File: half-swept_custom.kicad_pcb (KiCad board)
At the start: 2 copper layers, 108.6 x 86.9 mm, 24 parts, among them J2 AudioJack4dpb, SW10 SW_Push, SW11 SW_Push, SW12 SW_Push, SW14 SW_Push, SW15 SW_Push, SW16 SW_Push, SW17 SW_Push, SW18 SW_Push, SW2 SW_Push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

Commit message: Add silkscreen switch picture to half-swept
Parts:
- added REF**: silk_pg1232_bottom, silkscreens:pg1232_bottom, B.Cu at (57.5, 76.0)
- added REF**: silk_pg2132_top, silkscreens:pg1232_top, F.Cu at (57.5, 75.0)

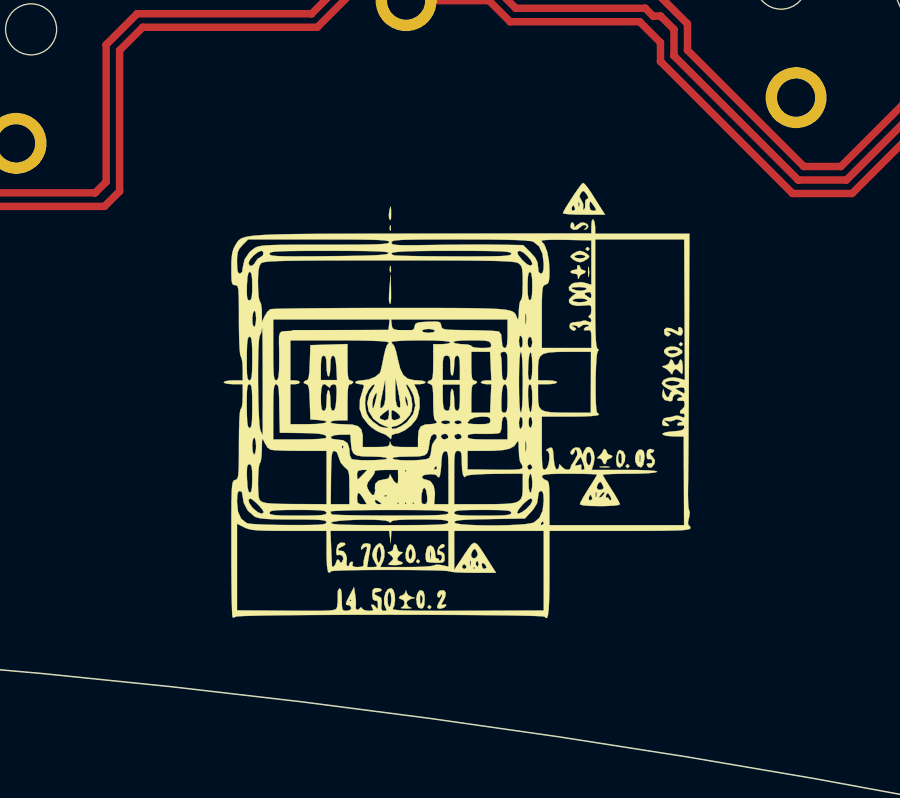
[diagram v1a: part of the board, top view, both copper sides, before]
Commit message: Add half swept boards with silkscreen
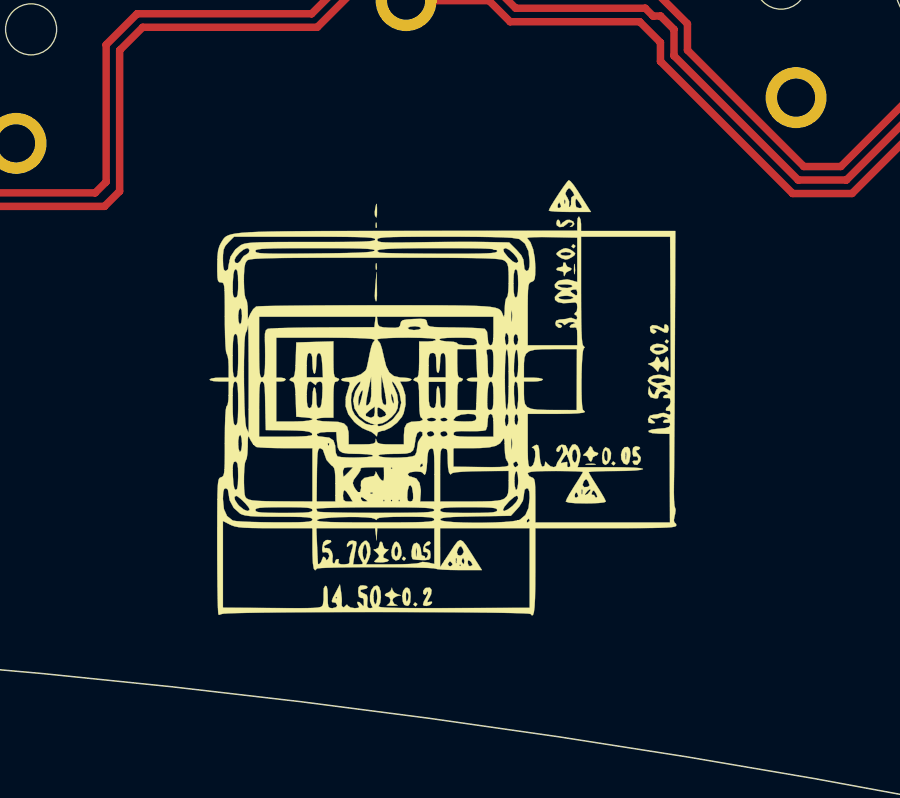
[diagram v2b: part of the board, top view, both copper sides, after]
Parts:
- moved REF** 1.66 mm to (59.1, 75.7)
- moved REF** 0.48 mm to (57.0, 74.9)

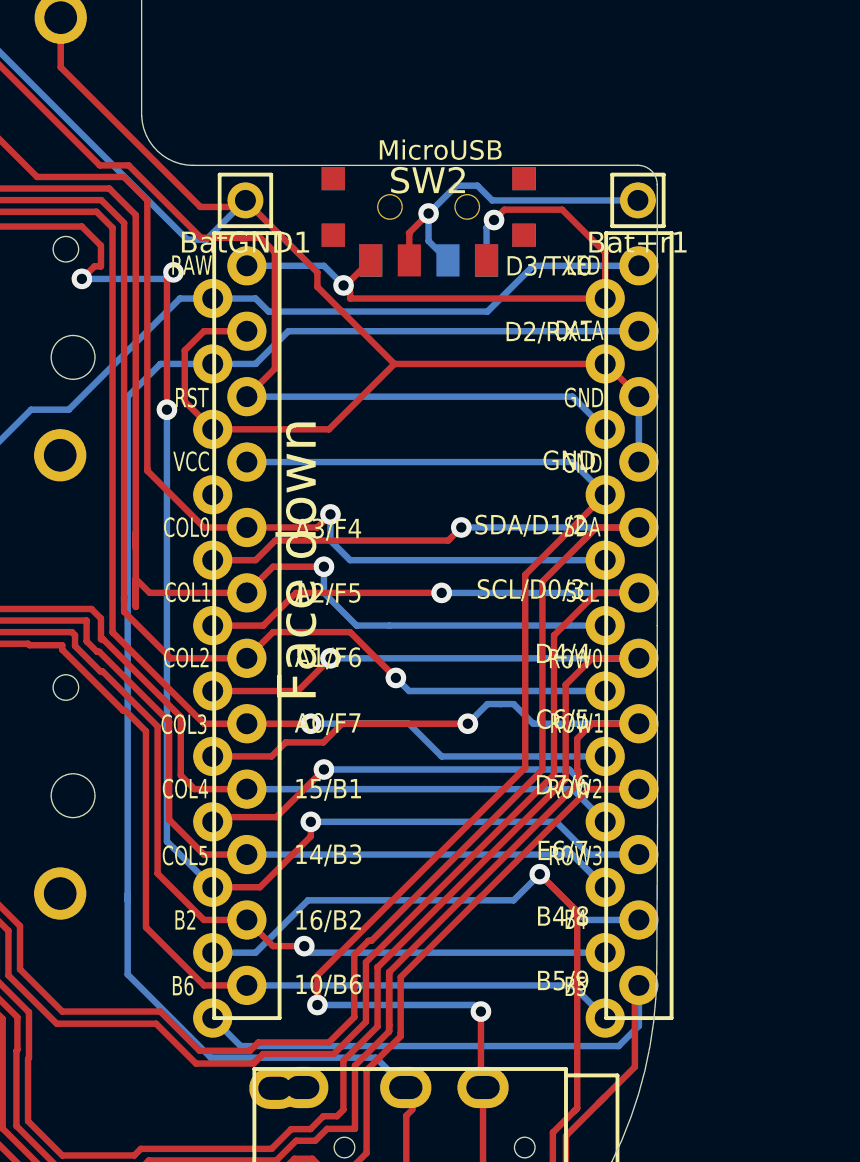
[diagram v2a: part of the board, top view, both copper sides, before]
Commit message: Remove battery pads and overlapping silkscreen
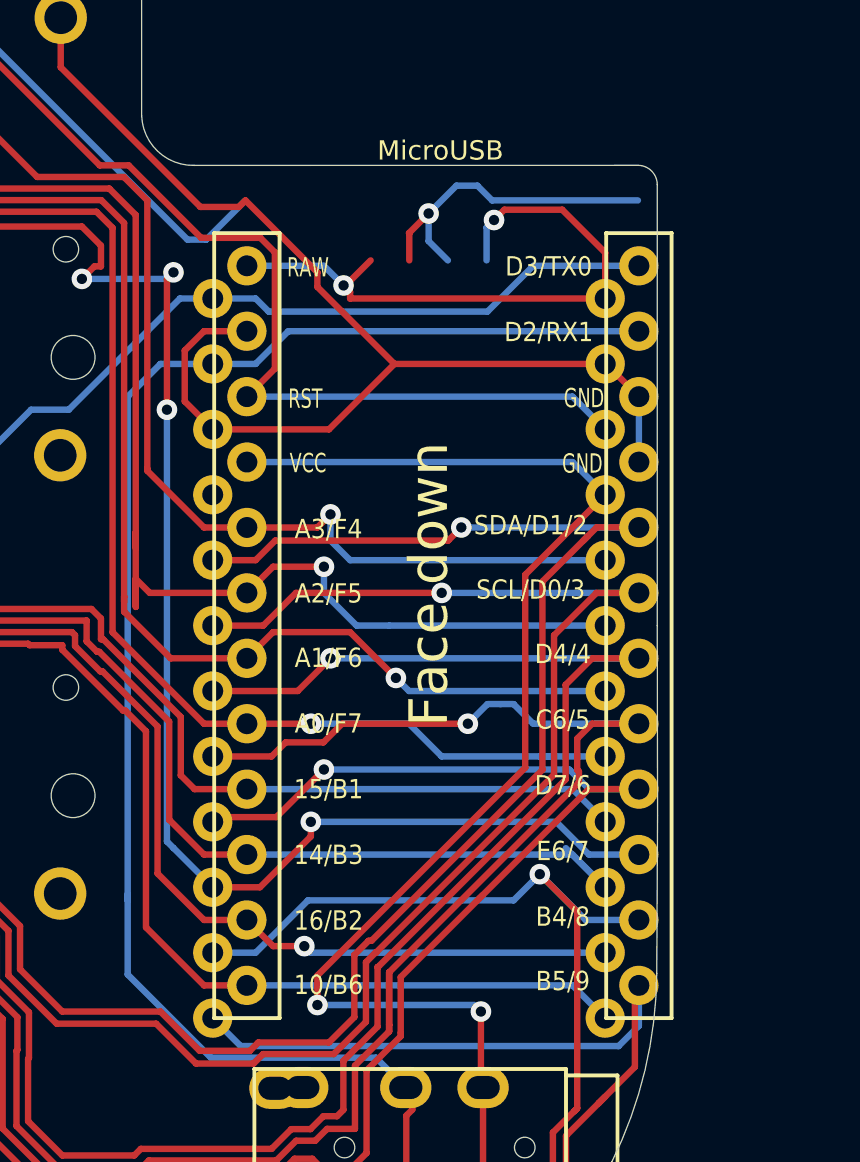
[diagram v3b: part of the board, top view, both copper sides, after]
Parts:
- removed Bat+r1, BatGND1: MountingHole_Pad, kbd:1pin_conn
- removed the SW2 at (113.3, 41.1)
- removed SW_POWERR1: SW_SPDT, Kailh:SPDT_C128955

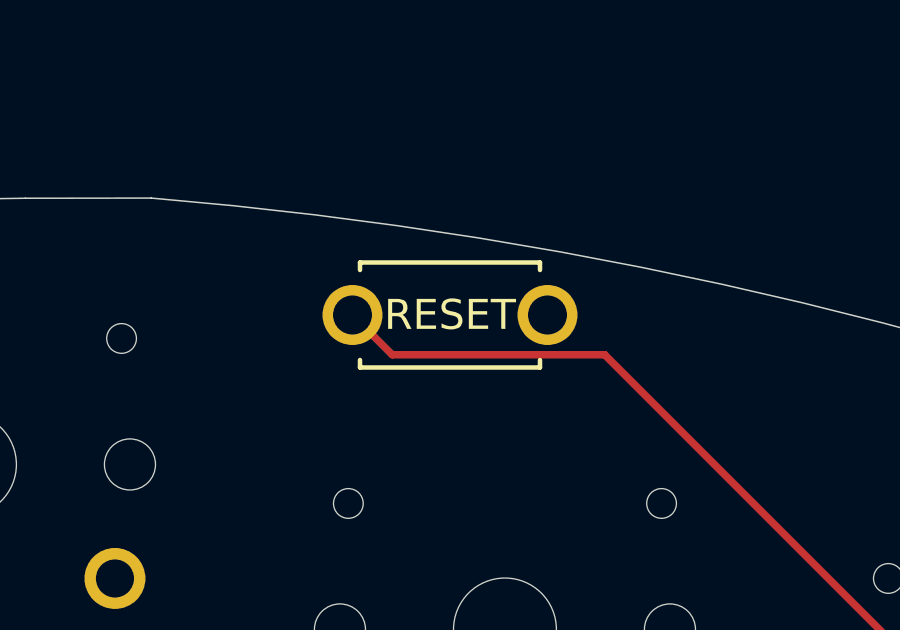
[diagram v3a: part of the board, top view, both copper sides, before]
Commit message: Remove reset switch
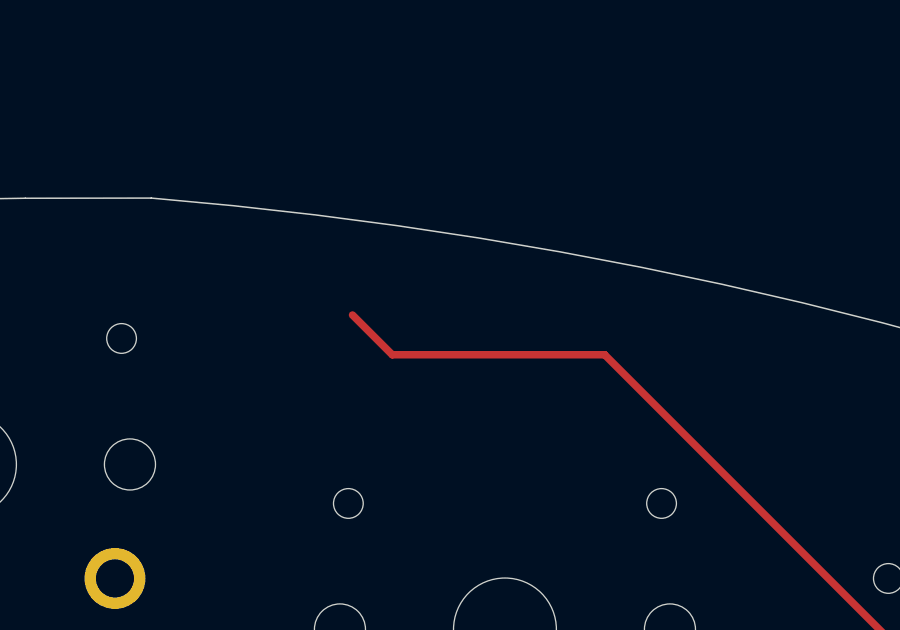
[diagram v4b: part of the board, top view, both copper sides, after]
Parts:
- removed RSW1: SW_Push, kbd:ResetSW

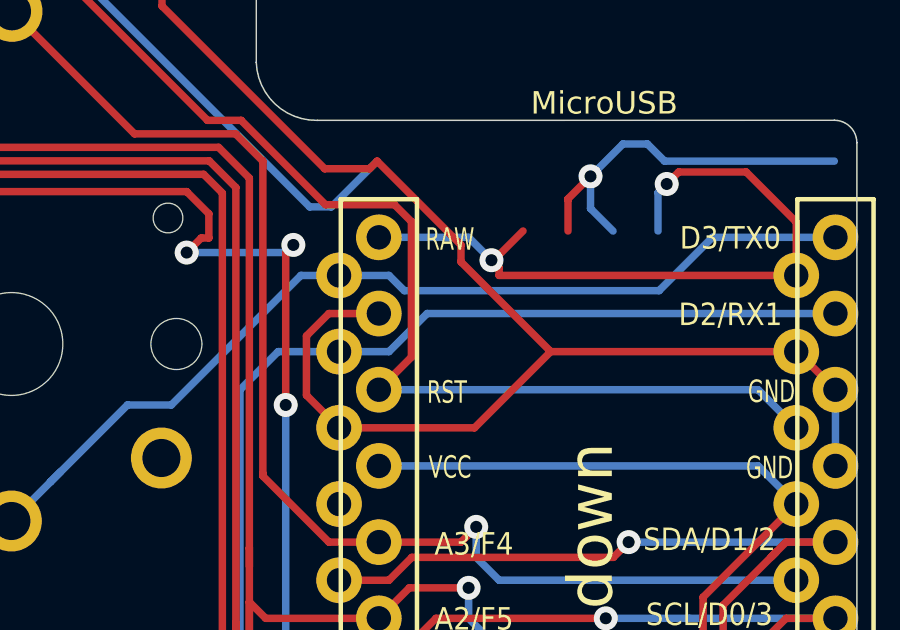
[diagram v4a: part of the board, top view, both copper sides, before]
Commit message: Add missing GND label
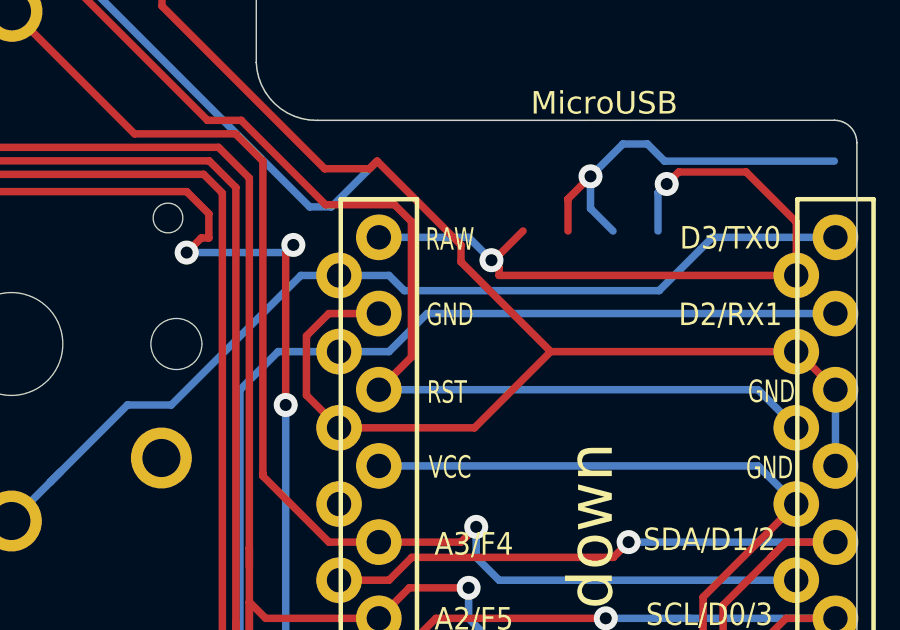
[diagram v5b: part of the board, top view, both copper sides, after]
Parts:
- added ?: , , F.Cu at (113.1, 56.1)
